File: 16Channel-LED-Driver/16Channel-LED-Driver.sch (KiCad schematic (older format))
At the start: 19 parts, among them P1 CONN_01X02, P10 CONN_01X02, P11 CONN_01X02, P12 CONN_01X02, P13 CONN_01X02, P14 CONN_01X02, P2 CONN_01X06, P3 CONN_01X02, P4 CONN_01X02, P5 CONN_01X06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

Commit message: Did Revision B of the 16 Channel board, also exported some gerbers
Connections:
- net +12V-A is gone; now on net +12V: C1.1, P11.2 (P2), U1.1 (VIN), U1.3 (INH)
- net +12V-B is gone; now on net +12V: C2.1, P12.2 (P2), U2.1 (VIN), U2.3 (INH)
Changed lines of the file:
@@
 $EndComp
 Connection ~ 1700 2650
-Text Label 1700 1500 1    60   ~ 0
-+12V-A
-Text Label 1700 2650 1    60   ~ 0
-+12V-B
 $Comp
 L CONN_01X02 P14
@@
 Text GLabel 3900 3000 2    60   Input ~ 0
 +5V-B
+$Comp
+L +12V #PWR011
+U 1 1 5976ACA2
+P 1550 2650
+F 0 "#PWR011" H 1550 2500 50  0001 C CNN
+F 1 "+12V" H 1550 2790 50  0000 C CNN
+F 2 "" H 1550 2650 50  0000 C CNN
+F 3 "" H 1550 2650 50  0000 C CNN
+	1    1550 2650
+	1    0    0    -1
+$EndComp
+Connection ~ 1550 2650
+$Comp
+L +12V #PWR012
+U 1 1 5976AD13
+P 1550 1500
+F 0 "#PWR012" H 1550 1350 50  0001 C CNN
+F 1 "+12V" H 1550 1640 50  0000 C CNN
+F 2 "" H 1550 1500 50  0000 C CNN
+F 3 "" H 1550 1500 50  0000 C CNN
+	1    1550 1500
+	1    0    0    -1
+$EndComp
+Connection ~ 1550 1500
 $EndSCHEMATC

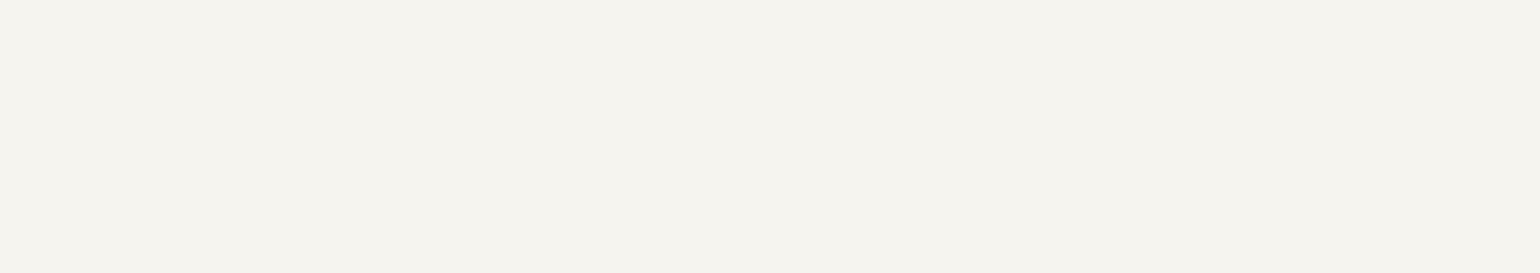
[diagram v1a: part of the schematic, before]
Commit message: Did third and hopefully final revision of the 16 channel LED board. I like making dumb mistakes. :(
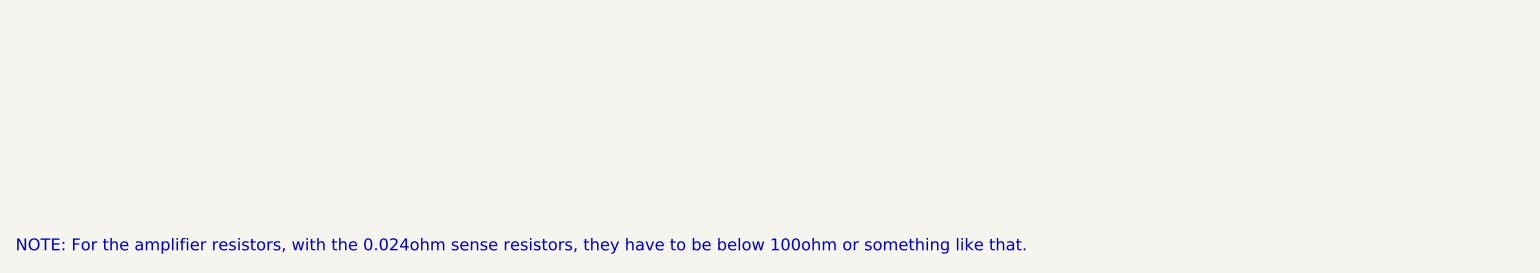
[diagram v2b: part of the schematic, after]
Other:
- note added: "NOTE: For the amplifier resistors, with the 0.024ohm sense resistors, they have to be below 100ohm or something like that."
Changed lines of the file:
@@
 NoConn ~ 2850 2750
 $Comp
-L GND #PWR01
+L GND #PWR10
 U 1 1 588BA47F
 P 2350 3100
-F 0 "#PWR01" H 2350 2850 50  0001 C CNN
+F 0 "#PWR10" H 2350 2850 50  0001 C CNN
 F 1 "GND" H 2350 2950 50  0000 C CNN
 F 2 "" H 2350 3100 50  0000 C CNN
@@
 NoConn ~ 2850 1600
 $Comp
-L GND #PWR02
+L GND #PWR5
 U 1 1 588BAADB
 P 2350 1950
-F 0 "#PWR02" H 2350 1700 50  0001 C CNN
+F 0 "#PWR5" H 2350 1700 50  0001 C CNN
 F 1 "GND" H 2350 1800 50  0000 C CNN
 F 2 "" H 2350 1950 50  0000 C CNN
@@
 Main Power Supply Connectors
 $Comp
-L +12V #PWR03
+L +12V #PWR1
 U 1 1 588BB609
 P 4400 1150
-F 0 "#PWR03" H 4400 1000 50  0001 C CNN
+F 0 "#PWR1" H 4400 1000 50  0001 C CNN
 F 1 "+12V" H 4400 1290 50  0000 C CNN
 F 2 "" H 4400 1150 50  0000 C CNN
@@
 $EndComp
 $Comp
-L GND #PWR04
+L GND #PWR4
 U 1 1 588BB62D
 P 5300 1650
-F 0 "#PWR04" H 5300 1400 50  0001 C CNN
+F 0 "#PWR4" H 5300 1400 50  0001 C CNN
 F 1 "GND" H 5300 1500 50  0000 C CNN
 F 2 "" H 5300 1650 50  0000 C CNN
@@
 $EndComp
 $Comp
-L +3V3 #PWR05
+L +3V3 #PWR11
 U 1 1 588C257B
 P 6150 4550
-F 0 "#PWR05" H 6150 4400 50  0001 C CNN
+F 0 "#PWR11" H 6150 4400 50  0001 C CNN
 F 1 "+3V3" H 6150 4690 50  0000 C CNN
 F 2 "" H 6150 4550 50  0000 C CNN
@@
 $EndComp
 $Comp
-L +3V3 #PWR06
+L +3V3 #PWR12
 U 1 1 588C288C
 P 6000 5450
-F 0 "#PWR06" H 6000 5300 50  0001 C CNN
+F 0 "#PWR12" H 6000 5300 50  0001 C CNN
 F 1 "+3V3" H 6000 5590 50  0000 C CNN
 F 2 "" H 6000 5450 50  0000 C CNN
@@
 Connection ~ 1700 1500
 $Comp
-L GND #PWR07
+L GND #PWR3
 U 1 1 58900721
 P 1400 1600
-F 0 "#PWR07" H 1400 1350 50  0001 C CNN
+F 0 "#PWR3" H 1400 1350 50  0001 C CNN
 F 1 "GND" H 1400 1450 50  0000 C CNN
 F 2 "" H 1400 1600 50  0000 C CNN
@@
 $EndComp
 $Comp
-L GND #PWR08
+L GND #PWR8
 U 1 1 5890077B
 P 1400 2750
-F 0 "#PWR08" H 1400 2500 50  0001 C CNN
+F 0 "#PWR8" H 1400 2500 50  0001 C CNN
 F 1 "GND" H 1400 2600 50  0000 C CNN
 F 2 "" H 1400 2750 50  0000 C CNN
@@
 $EndComp
 $Comp
-L GND #PWR09
+L GND #PWR6
 U 1 1 5890D552
 P 3750 1950
-F 0 "#PWR09" H 3750 1700 50  0001 C CNN
+F 0 "#PWR6" H 3750 1700 50  0001 C CNN
 F 1 "GND" H 3750 1800 50  0000 C CNN
 F 2 "" H 3750 1950 50  0000 C CNN
@@
 $EndComp
 $Comp
-L GND #PWR010
+L GND #PWR9
 U 1 1 5890D5B0
 P 3800 3000
-F 0 "#PWR010" H 3800 2750 50  0001 C CNN
+F 0 "#PWR9" H 3800 2750 50  0001 C CNN
 F 1 "GND" H 3800 2850 50  0000 C CNN
 F 2 "" H 3800 3000 50  0000 C CNN
@@
 +5V-B
 $Comp
-L +12V #PWR011
+L +12V #PWR7
 U 1 1 5976ACA2
 P 1550 2650
-F 0 "#PWR011" H 1550 2500 50  0001 C CNN
+F 0 "#PWR7" H 1550 2500 50  0001 C CNN
 F 1 "+12V" H 1550 2790 50  0000 C CNN
 F 2 "" H 1550 2650 50  0000 C CNN
@@
 Connection ~ 1550 2650
 $Comp
-L +12V #PWR012
+L +12V #PWR2
 U 1 1 5976AD13
 P 1550 1500
-F 0 "#PWR012" H 1550 1350 50  0001 C CNN
+F 0 "#PWR2" H 1550 1350 50  0001 C CNN
 F 1 "+12V" H 1550 1640 50  0000 C CNN
 F 2 "" H 1550 1500 50  0000 C CNN
@@
 $EndComp
 Connection ~ 1550 1500
+Text Notes 900  7050 0    60   ~ 0
+NOTE: For the amplifier resistors, with the 0.024ohm sense resistors, they have to be below 100ohm or something like that.
 $EndSCHEMATC
